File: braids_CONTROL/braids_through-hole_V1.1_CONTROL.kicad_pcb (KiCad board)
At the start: 2 copper layers, 78.7 x 96 mm, 54 parts, among them IC1 74HC595N, IC2 74HC595N, IC8 LM4040-10.0, Q1 2N3904, Q2 2N3904, Q3 2N3904, Q4 2N3904, SW1 EC12E_SW

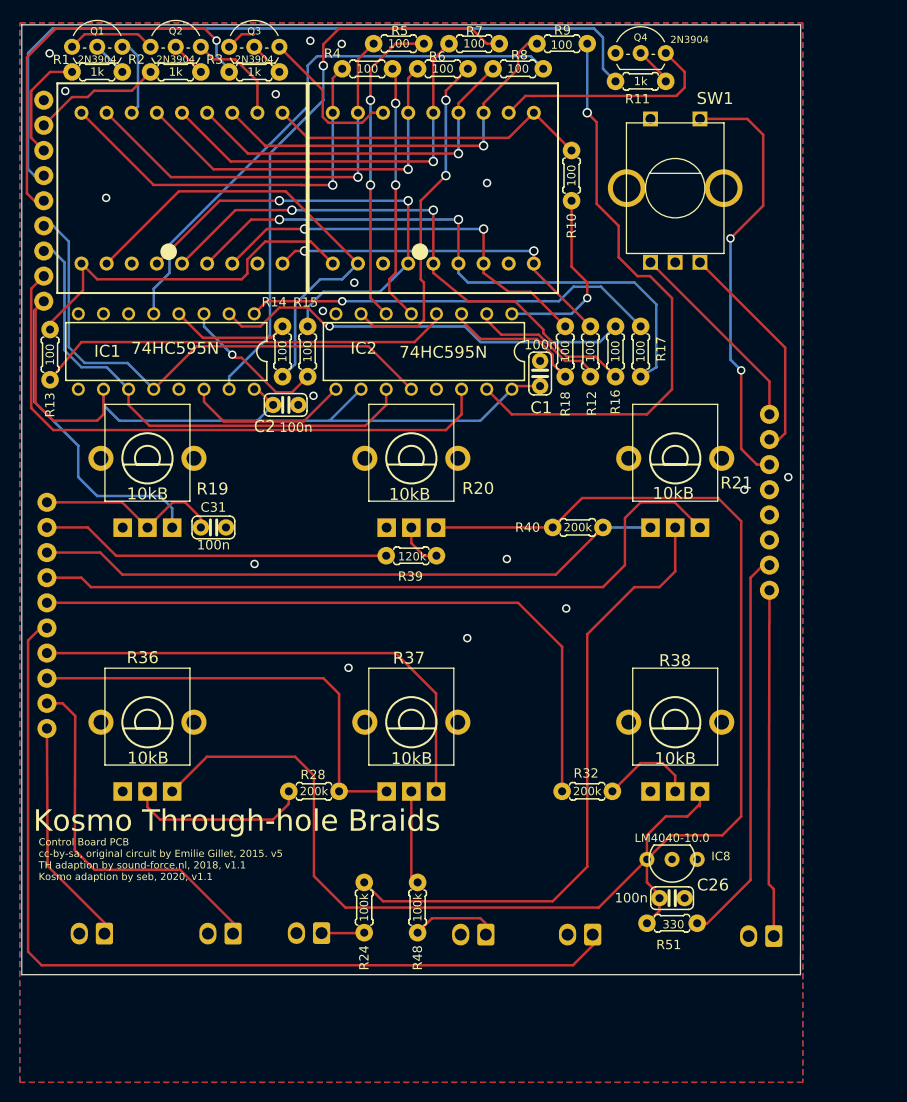
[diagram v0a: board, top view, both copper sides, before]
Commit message: add trim switch
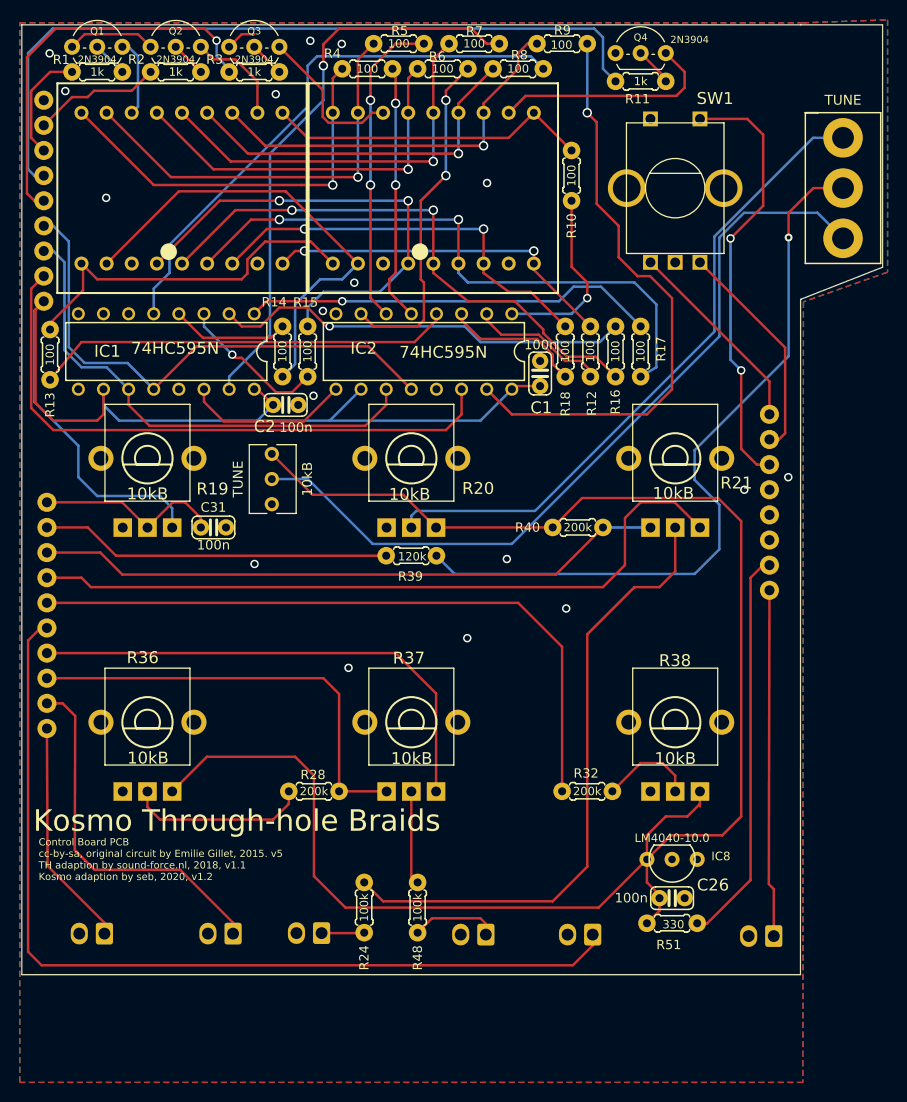
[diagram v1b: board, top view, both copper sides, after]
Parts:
- added TUNE: SPST SWITCH, lfo:SPDT SWITCH, F.Cu at (192.0, 68.0)
- added TUNE: 10kB, Potentiometer_THT:Potentiometer_Bourns_3266Y_Vertical, F.Cu at (134.3, 94.9)
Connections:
- R20 pad P$2: N$13 -> coarse_knob
- R39 pad 1: N$13 -> tune_sel
- R40 pad 1: AREF_-10 -> (no net)
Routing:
- net trim: track 0.00 -> 81.2 mm
- net tune_sel: track 0.00 -> 75.9 mm, vias 0 -> 1
- net coarse_knob: track 0.00 -> 66.3 mm
- net AREF_-10: track 156.2 -> 175.8 mm
- net N$13: track 4.64 -> 0.00 mm
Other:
- board size 78.7 x 96 mm -> 87 x 96 mm
- board text added: "Control Board PCB cc-by-sa, original circuit by Emilie Gillet, 2015. v5 TH adaption by sound-force.nl, 2018, v1.1 Kosmo adaption by seb, 2020, v1.2"
- board text removed: "Control Board PCB cc-by-sa, original circuit by Emilie Gillet, 2015. v5 TH adaption by sound-force.nl, 2018, v1.1 Kosmo adaption by seb, 2020, v1.1"
